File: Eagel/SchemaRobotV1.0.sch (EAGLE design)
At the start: 17 parts

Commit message: schema
schema bijna af
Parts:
- removed R6, R7: (no value), eagle-ltspice:R0204/7
- added C1, C2: (no value), rcl:C-EU025-024X044
- added Q1: (no value), special:XTAL
- added S3: (no value), switch-dil:DS01E
- added SV3, SV4, SV5: (no value), con-amp-mt:L05P
- added SV6: (no value), con-amp-mt:L08P
- added SV7: (no value), con-amp-mt:L02P
- added SV8: (no value), con-amp-mt:L16P
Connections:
- removed net IRS5: DEVICE1.P2.4
- removed net N$1: DEVICE1.P3.3, LED1.A
- removed net N$19: DEVICE1.VDD, S1.2, S2.2, SV1-11.S, SV2-2.S
- removed net N$7: DEVICE1.P3.4, LED2.A
- new net ECHO: DEVICE1.P1.0/SWDIO, DEVICE1.P12.1/I2C(SDA), DEVICE1.P12.3, SV3-2.S, SV4-2.S, SV5-2.S
- new net ENA: DEVICE1.P1.2, SV6-1.S
- new net ENB: DEVICE1.P1.7, SV6-6.S
- new net IN1: DEVICE1.P1.3, SV6-2.S
- new net IN2: DEVICE1.P1.4, SV6-3.S
- new net IN3: DEVICE1.P1.5, SV6-4.S
- new net IN4: DEVICE1.P1.6, SV6-5.S
- new net LED1: DEVICE1.P3.0, LED1.A
- new net LED2: DEVICE1.P3.1, LED2.A
- new net LED3: DEVICE1.P3.2/EXT_REF1, LED3.A
- new net LED4: DEVICE1.P3.3, LED4.A
- new net LED5: DEVICE1.P3.4, LED5.A
- new net LEDON: DEVICE1.P2.0, SV1-2.S
- new net N$13: S3.1, SV7-1.S
- new net N$14: S3.2, SV7-2.S
- new net N$15: DEVICE1.P0.1, SV8-13.S
- new net N$16: DEVICE1.P0.0, SV8-14.S
- new net N$17: C1.1, DEVICE1.P15.2/XTAL_OUT, Q1.1
- new net N$18: C2.1, DEVICE1.P15.3/XTAL_IN, Q1.2
- new net SW1: DEVICE1.P3.5, S2.1
- new net SW2: DEVICE1.P3.6, S1.1
- new net TRIG: DEVICE1.P1.1/SWDCLK, DEVICE1.P12.0/I2C(SCL), DEVICE1.P12.2, SV3-3.S, SV4-3.S, SV5-3.S
- new net VCC: DEVICE1.VDD, S1.2, S2.2, SV1-1.S, SV3-1.S, SV4-1.S, SV5-1.S, SV6-8.S, SV8-2.S
- new net VCCIN: SV2-2.S
- net GND: now also C1.2, C2.2, SV1-11.S, SV3-5.S, SV4-5.S, SV5-5.S, SV6-7.S, SV8-1.S, SV8-3.S; no longer R6.1, SV1-2.S
- net IRS: now also DEVICE1.P2.3; no longer DEVICE1.P2.2/SW1
- net IRS1: now also DEVICE1.P2.1/LED1; no longer DEVICE1.P2.0
- net IRS2: now also DEVICE1.P2.2/SW1; no longer DEVICE1.P2.1/LED1
- net IRS4: no longer DEVICE1.P2.3
- net IRS6: now also DEVICE1.P2.6; no longer DEVICE1.P2.5
- net IRS7: now also DEVICE1.P2.7; no longer DEVICE1.P2.6
- net N$10: now also DEVICE1.P0.4/SAR0, SV8-6.S; no longer DEVICE1.P3.7, LED5.A
- net N$11: now also DEVICE1.P0.3/EXT_REF0, SV8-11.S; no longer DEVICE1.P12.5, R6.2, S1.1
- net N$12: now also DEVICE1.P0.2/SAR1, SV8-12.S; no longer S2.1
- net N$8: now also DEVICE1.P0.6, SV8-4.S; no longer DEVICE1.P3.5, LED3.A
- net N$9: now also DEVICE1.P0.5, SV8-5.S; no longer DEVICE1.P3.6, LED4.A
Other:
- note added: "Connector H-Brug (signalen)"
- note added: "Connector IR sensoren"
- note added: "Connector LCD"
- note added: "Connector US 1"
- note added: "Connector US 2"
- note added: "Connector US 3"
- note added: "Connector batterij"
- note added: "Connector h-brug (voeding) NIET MEER NODIG"
- moved on the sheet: LED1, LED2, LED3, LED4, LED5, R1, R2, R3, R4, R5, S1, S2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

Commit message: eagle
schema
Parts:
- removed SV2: (no value), con-amp-mt:L02P
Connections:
- removed net VCCIN: SV2-2.S
- net GND: now also R2.1, R3.1, R4.1, R5.1; no longer SV2-1.S
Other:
- note removed: "Connector h-brug (voeding) NIET MEER NODIG"
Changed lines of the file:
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@@
 <part name="GND4" library="supply1" library_urn="urn:adsk.eagle:library:371" deviceset="GND" device=""/>
 <part name="GND5" library="supply1" library_urn="urn:adsk.eagle:library:371" deviceset="GND" device=""/>
-<part name="SV2" library="con-amp-mt" library_urn="urn:adsk.eagle:library:123" deviceset="L02P" device="" package3d_urn="urn:adsk.eagle:package:5777/1"/>
 <part name="S1" library="switch-dil" library_urn="urn:adsk.eagle:library:375" deviceset="DS01E" device="" package3d_urn="urn:adsk.eagle:package:27201/2"/>
 <part name="S2" library="switch-dil" library_urn="urn:adsk.eagle:library:375" deviceset="DS01E" device="" package3d_urn="urn:adsk.eagle:package:27201/2"/>
@@
 <part name="P+4" library="supply1" library_urn="urn:adsk.eagle:library:371" deviceset="VCC" device=""/>
 <part name="P+5" library="supply1" library_urn="urn:adsk.eagle:library:371" deviceset="VCC" device=""/>
-<part name="GND9" library="supply1" library_urn="urn:adsk.eagle:library:371" deviceset="GND" device=""/>
-<part name="P+6" library="supply1" library_urn="urn:adsk.eagle:library:371" deviceset="VCC" device=""/>
 <part name="P+7" library="supply1" library_urn="urn:adsk.eagle:library:371" deviceset="VCC" device=""/>
 <part name="P+8" library="supply1" library_urn="urn:adsk.eagle:library:371" deviceset="VCC" device=""/>
@@
 <text x="40.64" y="15.24" size="1.778" layer="91">Connector batterij</text>
 <text x="-30.48" y="205.74" size="1.778" layer="91">Connector IR sensoren</text>
-<text x="71.12" y="241.3" size="1.778" layer="91">Connector h-brug (voeding) NIET MEER NODIG</text>
 <text x="-76.2" y="147.32" size="1.778" layer="91" rot="MR0">Connector US 1</text>
 <text x="-76.2" y="88.9" size="1.778" layer="91" rot="MR0">Connector US 2</text>
@@
 <instance part="GND4" gate="1" x="93.98" y="58.42"/>
 <instance part="GND5" gate="1" x="27.94" y="63.5"/>
-<instance part="SV2" gate="-1" x="86.36" y="231.14" rot="R180"/>
-<instance part="SV2" gate="-2" x="86.36" y="236.22" rot="R180"/>
 <instance part="S1" gate="1" x="147.32" y="83.82" rot="R270"/>
 <instance part="S2" gate="1" x="147.32" y="78.74" rot="R270"/>
@@
 <instance part="P+4" gate="VCC" x="-15.24" y="193.04"/>
 <instance part="P+5" gate="VCC" x="91.44" y="144.78"/>
-<instance part="GND9" gate="1" x="78.74" y="226.06"/>
-<instance part="P+6" gate="VCC" x="68.58" y="241.3"/>
 <instance part="P+7" gate="VCC" x="154.94" y="93.98"/>
 <instance part="P+8" gate="VCC" x="162.56" y="93.98"/>
@@
 <wire x1="101.6" y1="40.64" x2="101.6" y2="33.02" width="0.1524" layer="91"/>
 <wire x1="101.6" y1="33.02" x2="101.6" y2="27.94" width="0.1524" layer="91"/>
-<wire x1="109.22" y1="38.1" x2="109.22" y2="33.02" width="0.1524" layer="91"/>
+<wire x1="109.22" y1="40.64" x2="109.22" y2="33.02" width="0.1524" layer="91"/>
 <wire x1="109.22" y1="33.02" x2="101.6" y2="33.02" width="0.1524" layer="91"/>
-<wire x1="132.08" y1="38.1" x2="132.08" y2="33.02" width="0.1524" layer="91"/>
+<wire x1="132.08" y1="40.64" x2="132.08" y2="33.02" width="0.1524" layer="91"/>
 <wire x1="132.08" y1="33.02" x2="124.46" y2="33.02" width="0.1524" layer="91"/>
 <wire x1="124.46" y1="33.02" x2="116.84" y2="33.02" width="0.1524" layer="91"/>
 <wire x1="116.84" y1="33.02" x2="109.22" y2="33.02" width="0.1524" layer="91"/>
-<wire x1="124.46" y1="38.1" x2="124.46" y2="33.02" width="0.1524" layer="91"/>
-<wire x1="116.84" y1="38.1" x2="116.84" y2="33.02" width="0.1524" layer="91"/>
+<wire x1="124.46" y1="40.64" x2="124.46" y2="33.02" width="0.1524" layer="91"/>
+<wire x1="116.84" y1="40.64" x2="116.84" y2="33.02" width="0.1524" layer="91"/>
 <junction x="101.6" y="33.02"/>
 <junction x="109.22" y="33.02"/>
 <junction x="116.84" y="33.02"/>
 <junction x="124.46" y="33.02"/>
+<pinref part="R2" gate="G$1" pin="1"/>
+<pinref part="R4" gate="G$1" pin="1"/>
+<pinref part="R3" gate="G$1" pin="1"/>
+<pinref part="R5" gate="G$1" pin="1"/>
 </segment>
 <segment>
@@
 <wire x1="83.82" y1="134.62" x2="91.44" y2="134.62" width="0.1524" layer="91"/>
 <wire x1="91.44" y1="134.62" x2="91.44" y2="132.08" width="0.1524" layer="91"/>
-</segment>
-<segment>
-<pinref part="GND9" gate="1" pin="GND"/>
-<wire x1="78.74" y1="231.14" x2="78.74" y2="228.6" width="0.1524" layer="91"/>
-<pinref part="SV2" gate="-1" pin="S"/>
-<wire x1="78.74" y1="231.14" x2="81.28" y2="231.14" width="0.1524" layer="91"/>
 </segment>
 <segment>
@@
 </segment>
 </net>
-<net name="VCCIN" class="0">
-<segment>
-<pinref part="P+6" gate="VCC" pin="VCC"/>
-<wire x1="68.58" y1="238.76" x2="68.58" y2="236.22" width="0.1524" layer="91"/>
-<wire x1="68.58" y1="236.22" x2="81.28" y2="236.22" width="0.1524" layer="91"/>
-<pinref part="SV2" gate="-2" pin="S"/>
-</segment>
-</net>

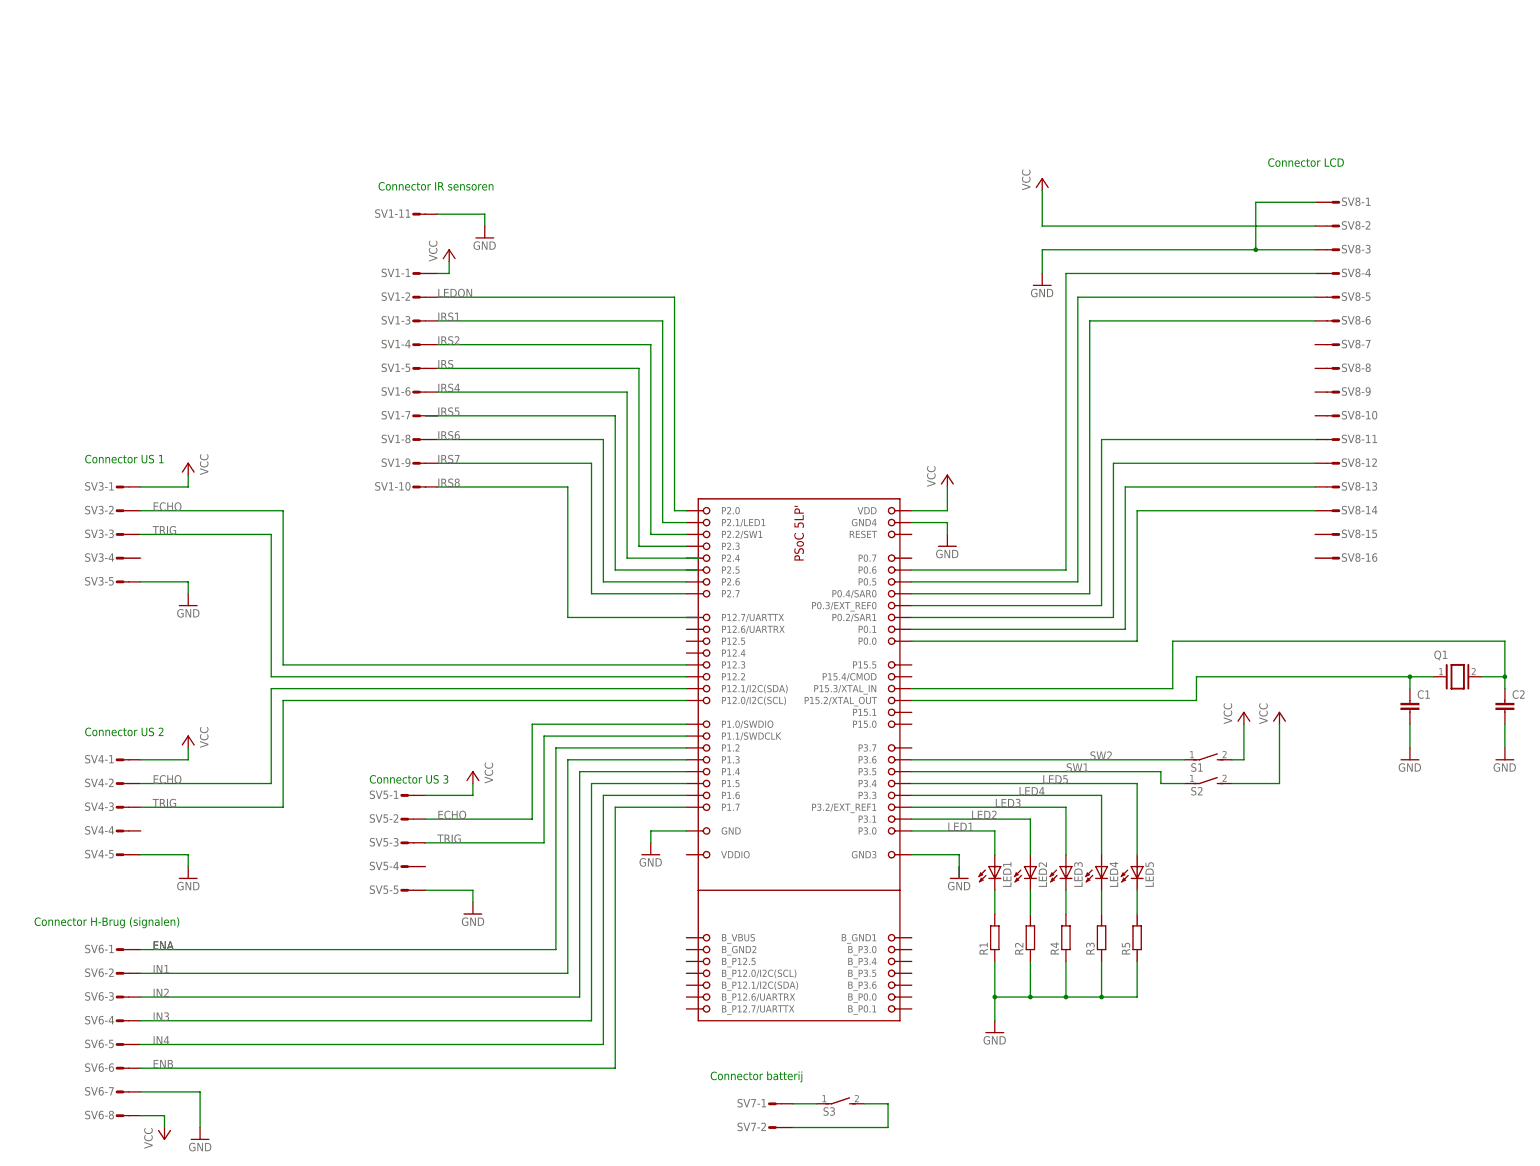
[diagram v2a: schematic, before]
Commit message: eagle
update schema
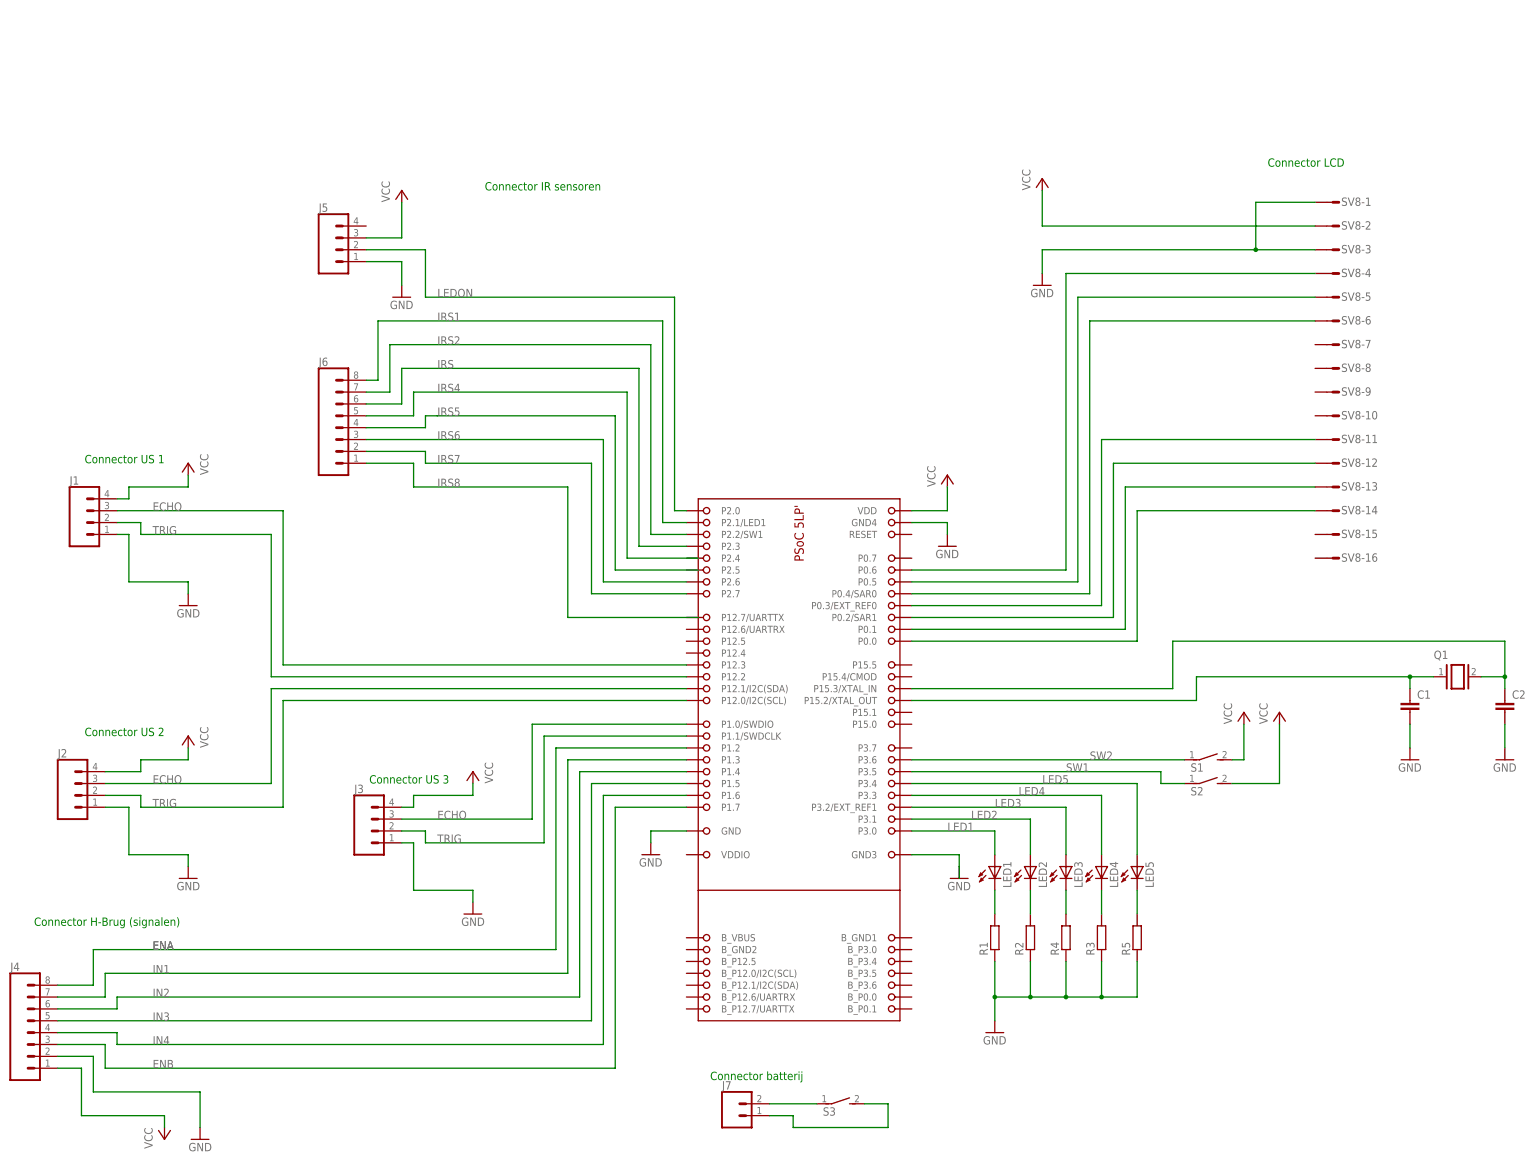
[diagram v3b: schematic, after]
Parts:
- removed SV1: (no value), con-amp-mt:L11P
- removed SV3, SV4, SV5: (no value), con-amp-mt:L05P
- removed SV6: (no value), con-amp-mt:L08P
- removed SV7: (no value), con-amp-mt:L02P
- added J1, J2, J3, J5: (no value), SparkFun-Connectors:CONN_04SCREW
- added J4, J6: (no value), SparkFun-Connectors:CONN_083.5MM-8
- added J7: (no value), SparkFun-Connectors:CONN_023.5MM
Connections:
- net ECHO: now also J1.3, J2.3, J3.3; no longer SV3-2.S, SV4-2.S, SV5-2.S
- net ENA: now also J4.8; no longer SV6-1.S
- net ENB: now also J4.3; no longer SV6-6.S
- net GND: now also J1.1, J2.1, J3.1, J4.2, J5.1; no longer SV1-11.S, SV3-5.S, SV4-5.S, SV5-5.S, SV6-7.S
- net IN1: now also J4.7; no longer SV6-2.S
- net IN2: now also J4.6; no longer SV6-3.S
- net IN3: now also J4.5; no longer SV6-4.S
- net IN4: now also J4.4; no longer SV6-5.S
- net IRS: now also J6.6; no longer SV1-5.S
- net IRS1: now also J6.8; no longer SV1-3.S
- net IRS2: now also J6.7; no longer SV1-4.S
- net IRS4: now also J6.5; no longer SV1-6.S
- net IRS6: now also J6.3; no longer SV1-8.S
- net IRS7: now also J6.2; no longer SV1-9.S
- net IRS8: now also J6.1; no longer SV1-10.S
- net LEDON: now also J5.2; no longer SV1-2.S
- net N$13: now also J7.2; no longer SV7-1.S
- net N$14: now also J7.1; no longer SV7-2.S
- net N$21: now also J6.4; no longer SV1-7.S
- net TRIG: now also J1.2, J2.2, J3.2; no longer SV3-3.S, SV4-3.S, SV5-3.S
- net VCC: now also J1.4, J2.4, J3.4, J4.1, J5.3; no longer SV1-1.S, SV3-1.S, SV4-1.S, SV5-1.S, SV6-8.S
